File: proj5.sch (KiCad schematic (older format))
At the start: 12 parts, among them SW1 SW_DIP_x01, U1 8284, U2 8086_Min_Mode, U3 74LS245, U4 74LS245, U5 74AHC373, U6 74AHC373, U7 74AHC373, Y1 Crystal

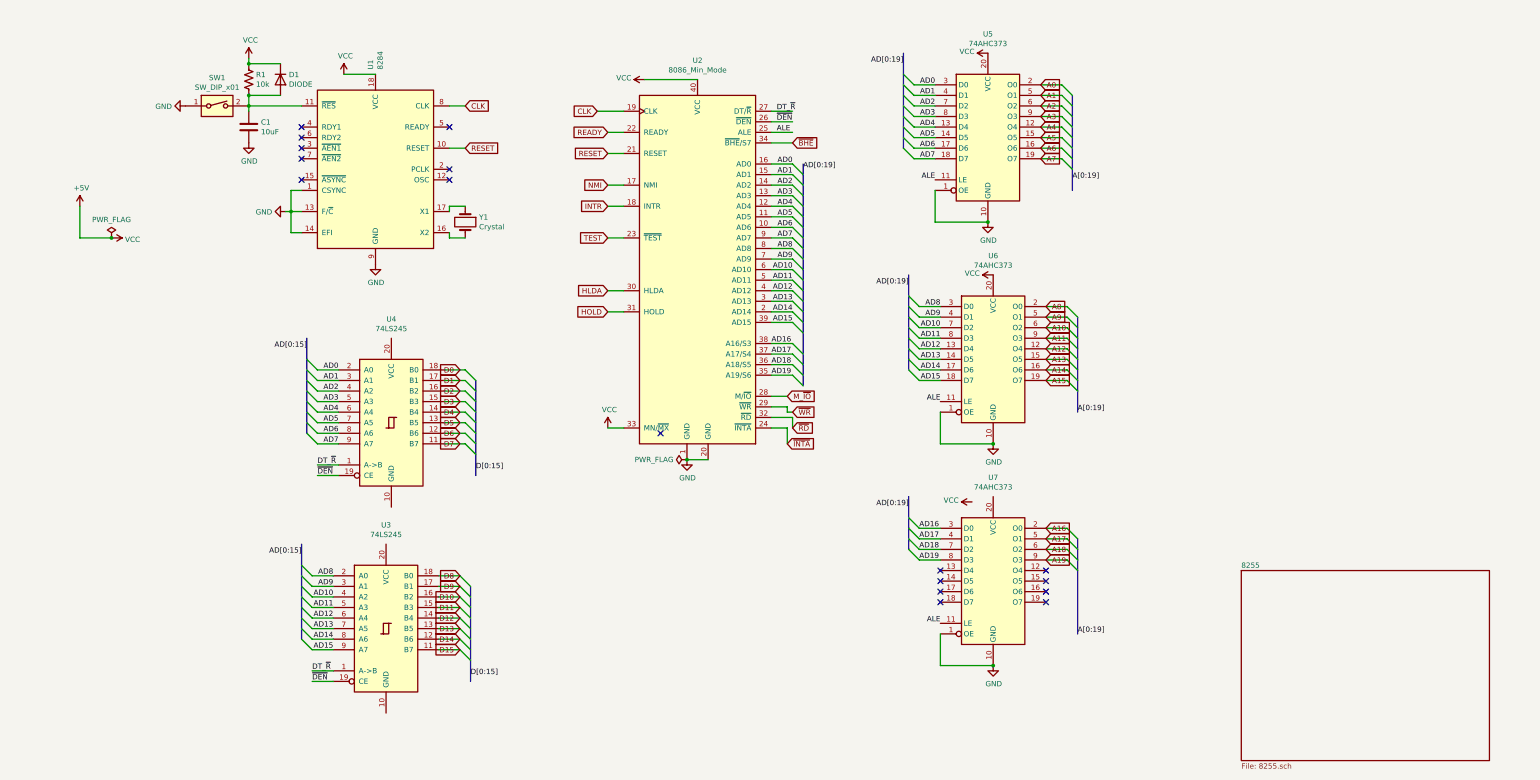
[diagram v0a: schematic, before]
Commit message: 8255 and 8060 schematics
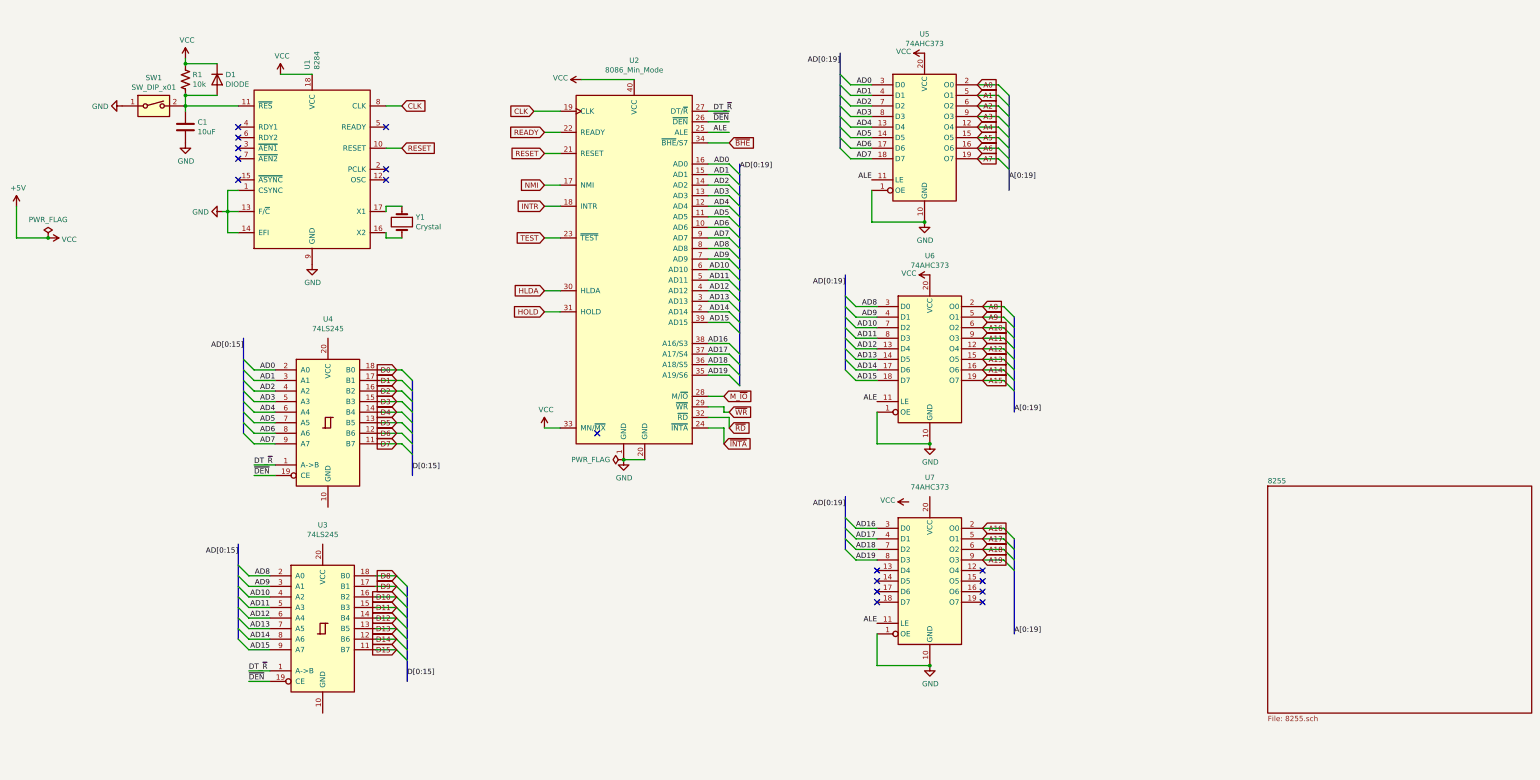
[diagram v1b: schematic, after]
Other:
- moved on the sheet: C1, D1, R1, SW1, U1, U2, U3, U4, U5, U6, U7, Y1

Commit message: updated 8086 and 8255 schematic
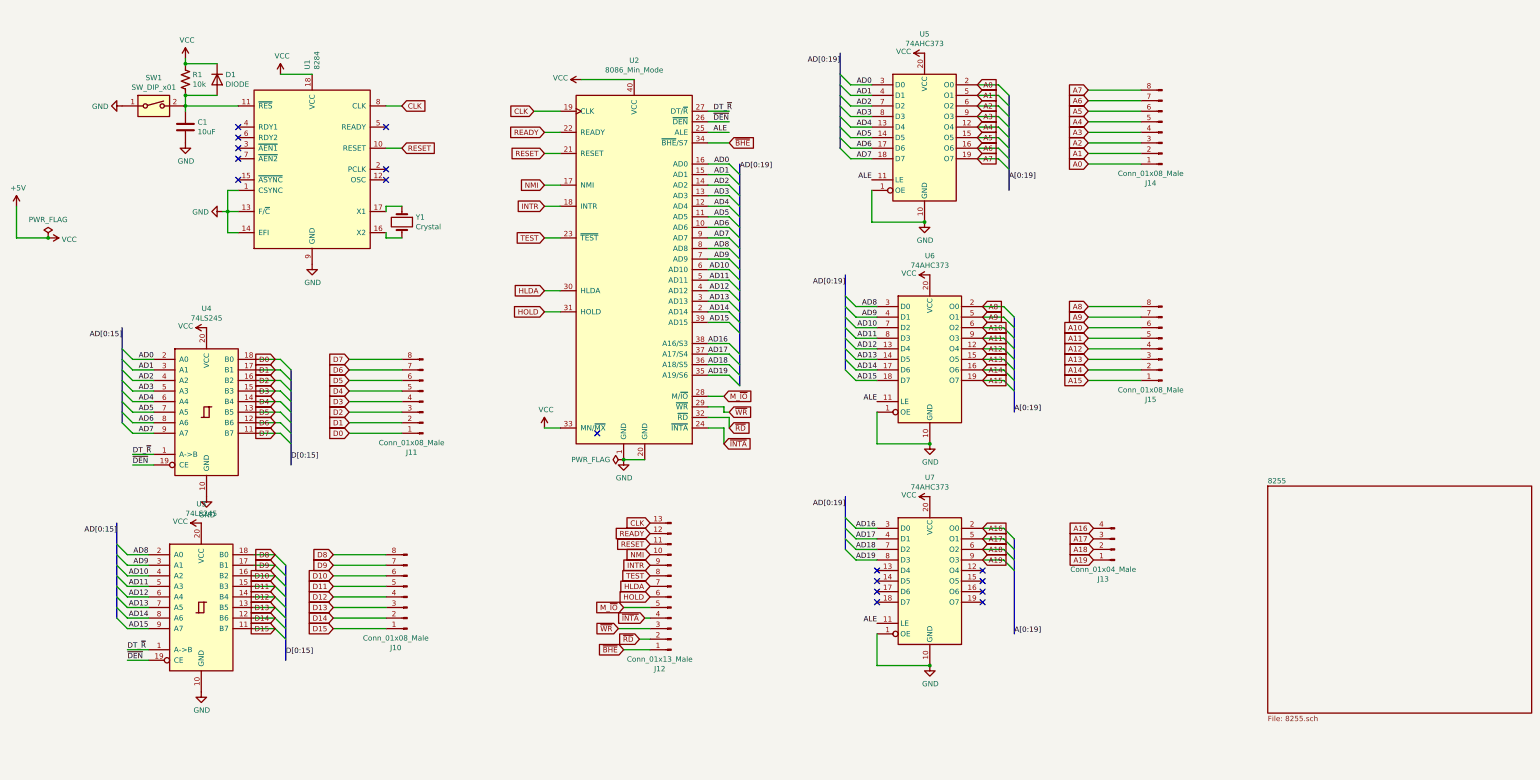
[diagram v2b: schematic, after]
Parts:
- added J10, J11, J14, J15: Conn_01x08_Male, symbol Connector:Conn_01x08_Male
- added J12: Conn_01x13_Male, symbol Connector:Conn_01x13_Male
- added J13: Conn_01x04_Male, symbol Connector:Conn_01x04_Male
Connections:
- net +5V: now also U3.20 (VCC), U4.20 (VCC), U7.20 (VCC)
- net A0: now also J14.1 (Pin_1)
- net A1: now also J14.2 (Pin_2)
- net A10: now also J15.6 (Pin_6)
- net A11: now also J15.5 (Pin_5)
- net A12: now also J15.4 (Pin_4)
- net A13: now also J15.3 (Pin_3)
- net A14: now also J15.2 (Pin_2)
- net A15: now also J15.1 (Pin_1)
- net A16: now also J13.4 (Pin_4)
- net A17: now also J13.3 (Pin_3)
- net A18: now also J13.2 (Pin_2)
- net A19: now also J13.1 (Pin_1)
- net A2: now also J14.3 (Pin_3)
- net A3: now also J14.4 (Pin_4)
- net A4: now also J14.5 (Pin_5)
- net A5: now also J14.6 (Pin_6)
- net A6: now also J14.7 (Pin_7)
- net A7: now also J14.8 (Pin_8)
- net A8: now also J15.8 (Pin_8)
- net A9: now also J15.7 (Pin_7)
- net CLK: now also J12.13 (Pin_13)
- net D0: now also J11.1 (Pin_1)
- net D1: now also J11.2 (Pin_2)
- net D10: now also J10.6 (Pin_6)
- net D11: now also J10.5 (Pin_5)
- net D12: now also J10.4 (Pin_4)
- net D13: now also J10.3 (Pin_3)
- net D14: now also J10.2 (Pin_2)
- net D15: now also J10.1 (Pin_1)
- net D2: now also J11.3 (Pin_3)
- net D3: now also J11.4 (Pin_4)
- net D4: now also J11.5 (Pin_5)
- net D5: now also J11.6 (Pin_6)
- net D6: now also J11.7 (Pin_7)
- net D7: now also J11.8 (Pin_8)
- net D8: now also J10.8 (Pin_8)
- net D9: now also J10.7 (Pin_7)
- net GND: now also U3.10 (GND), U4.10 (GND)
- net HLDA: now also J12.7 (Pin_7)
- net HOLD: now also J12.6 (Pin_6)
- net INTR: now also J12.9 (Pin_9)
- net M_~IO: now also J12.5 (Pin_5)
- net NMI: now also J12.10 (Pin_10)
- net READY: now also J12.12 (Pin_12)
- net RESET: now also J12.11 (Pin_11)
- net TEST: now also J12.8 (Pin_8)
- net ~BHE: now also J12.1 (Pin_1)
- net ~INTA: now also J12.4 (Pin_4)
- net ~RD: now also J12.2 (Pin_2)
- net ~WR: now also J12.3 (Pin_3)
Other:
- moved on the sheet: U3, U4

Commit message: Added 16550 UART
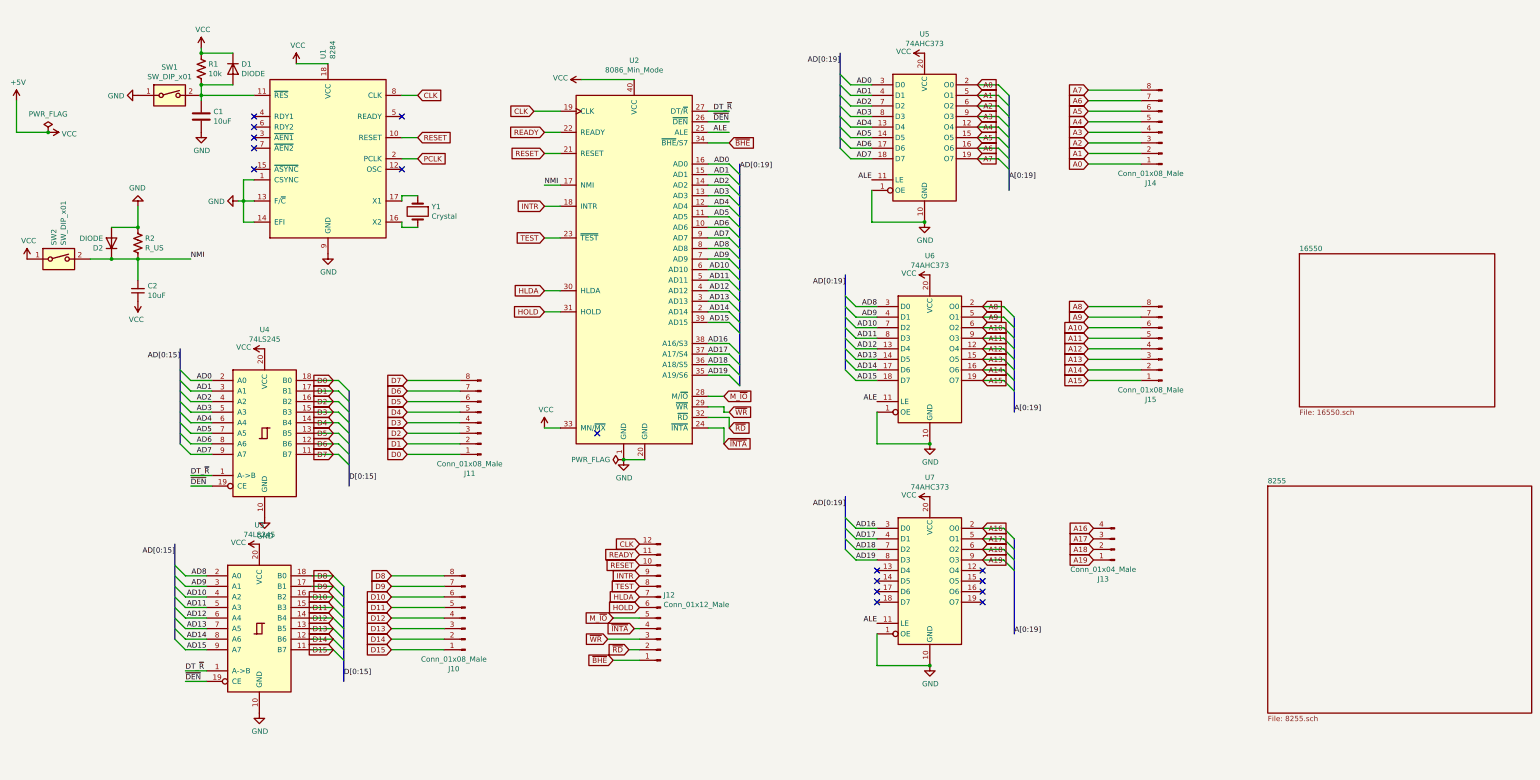
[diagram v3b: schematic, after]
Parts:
- removed J12: Conn_01x13_Male, symbol Connector:Conn_01x13_Male
- added C2: 10uF, symbol Device:C_Small
- added D2: DIODE, symbol Simulation_SPICE:DIODE
- added J12: Conn_01x12_Male, symbol Connector:Conn_01x12_Male
- added R2: R_US, symbol Device:R_US
- added SW2: SW_DIP_x01, symbol Switch:SW_DIP_x01
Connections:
- net +5V: now also C2.1, SW2.1
- net CLK: now also J12.12 (Pin_12)
- net GND: now also D2.1 (A), R2.1
- net HLDA: now also J12.7 (Pin_7)
- net HOLD: now also J12.6 (Pin_6)
- net INTR: now also J12.9 (Pin_9)
- net M_~IO: now also J12.5 (Pin_5)
- net NMI: now also C2.2, D2.2 (K), R2.2, SW2.2
- net READY: now also J12.11 (Pin_11)
- net RESET: now also J12.10 (Pin_10)
- net TEST: now also J12.8 (Pin_8)
- net ~BHE: now also J12.1 (Pin_1)
- net ~INTA: now also J12.4 (Pin_4)
- net ~RD: now also J12.2 (Pin_2)
- net ~WR: now also J12.3 (Pin_3)
- net PCLK: now reaches U1.2 (PCLK)
- no-connect marks 17 -> 16
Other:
- moved on the sheet: C1, D1, J10, J11, R1, SW1, U1, U3, U4, Y1

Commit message: update 16650
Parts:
- added C? (x2): 0.1uF, symbol Device:C
- added C?: 100uF, symbol Device:C
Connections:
- net +5V: now also C?.1, C?.2, C?.2
- net GND: now also C?.1, C?.1, C?.2
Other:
- moved on the sheet: U2
